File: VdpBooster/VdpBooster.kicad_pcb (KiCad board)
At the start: 2 copper layers, 36.2 x 73 mm, 30 parts, among them U1 M5M4C264L, U2 M5M4C264L, U3 M5M4C264L, U4 M5M4C264L, U5 315-5313A

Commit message: v101 changes
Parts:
- removed the C1 at (131.0, 65.5)
- removed the C2 at (137.0, 65.5)
- removed the C3 at (137.0, 53.5)
- removed the C4 at (131.0, 53.5)
- moved TP3 39.2 mm to (142.0, 13.9)
- moved TP4 35.3 mm to (145.0, 13.9)
- moved C4 32.5 mm to (138.6, 14.5), turned to 180 degrees
- moved C5 9.52 mm to (140.1, 74.5), turned to 180 degrees
- moved TP1 8.28 mm to (147.5, 87.2)
- moved TP7 8.19 mm to (133.5, 82.8)
- moved TP6 8.02 mm to (133.5, 79.8)
- moved TP5 7.98 mm to (133.5, 76.8)
- moved TP2 7.79 mm to (150.5, 87.2)
- moved R9 6.60 mm to (136.8, 83.5)
- moved C3 6.51 mm to (136.8, 82.0)
- moved R8 6.43 mm to (140.1, 83.5)
- moved R7 6.35 mm to (140.1, 82.0)
- moved R6 6.32 mm to (136.8, 80.5)
- moved C2 6.28 mm to (136.8, 79.0)
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- renumbered C6 to C1, C7 to C2, C8 to C3, C5 to C4, C9 to C5
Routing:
- net VCC: track 29.6 -> 72.8 mm, vias 0 -> 2
- net /A7: track 96.4 -> 123.9 mm, vias 2 -> 3
- net /A5: track 80.0 -> 107.1 mm, vias 1 -> 3
- net /A0: track 84.4 -> 110.9 mm
- net /A4: track 80.6 -> 106.5 mm, vias 1 -> 3
- net /A1: track 76.4 -> 102.3 mm, vias 1 -> 2
- net /A2: track 88.8 -> 111.7 mm
- net /A6: track 96.7 -> 119.3 mm, vias 1 -> 3
- net /A3: track 88.9 -> 110.5 mm
- net GND: track 36.5 -> 20.7 mm, vias 21 -> 20
- net /SC: track 78.5 -> 67.3 mm, vias 3 -> 2
- net /RD6: track 78.3 -> 69.7 mm, vias 2 -> 1
- net /RD2: track 80.0 -> 71.6 mm
- net /~{WE1}: track 56.0 -> 47.7 mm
- net /~{OE1}: track 66.8 -> 58.8 mm, vias 2 -> 1
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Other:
- board size 36.2 x 73 mm -> 34.9 x 76.4 mm
- board text added: "Analog VCC, GND⇢"
- board text added: "B"
- board text added: "G"
- board text added: "Human-made as always いつも通りAI不使用です"
- board text added: "R"
- board text added: "VDP BUDDY V1.0.1"
- board text added: "VRAM VCC, GND⇢"
- board text removed: "BLUE"
- board text removed: "GND"
- board text removed: "GNDA"
- board text removed: "GREEN"
- board text removed: "No AI/LLMs here! いつも通りAI不使用です"
- board text removed: "RED"
- board text removed: "VCC"
- board text removed: "VCCA"
- board text removed: "VDP BUDDY"
- board text removed: "←To CXA1145"

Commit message: tweaks and gerbils
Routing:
- net /SD4: track 65.2 -> 63.7 mm
- net /SD5: track 63.4 -> 62.5 mm
- net VCCA: track 30.2 -> 31.1 mm
- net /VID_B: track 8.97 -> 9.55 mm
- net /A7: track 123.9 -> 123.7 mm, vias 3 -> 2
- net GNDA: vias 16 -> 14

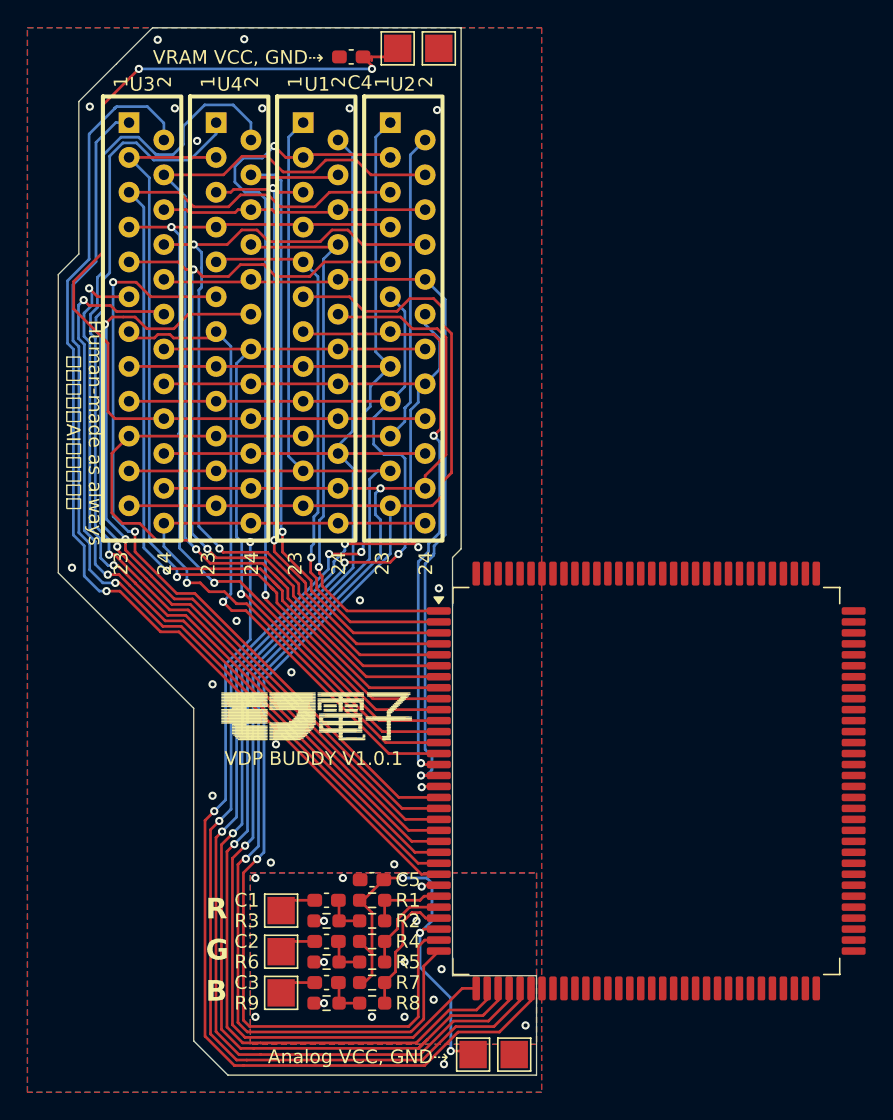
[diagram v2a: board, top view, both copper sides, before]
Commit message: Improved board layout, shrunk it and hopefully handled RGB Noise
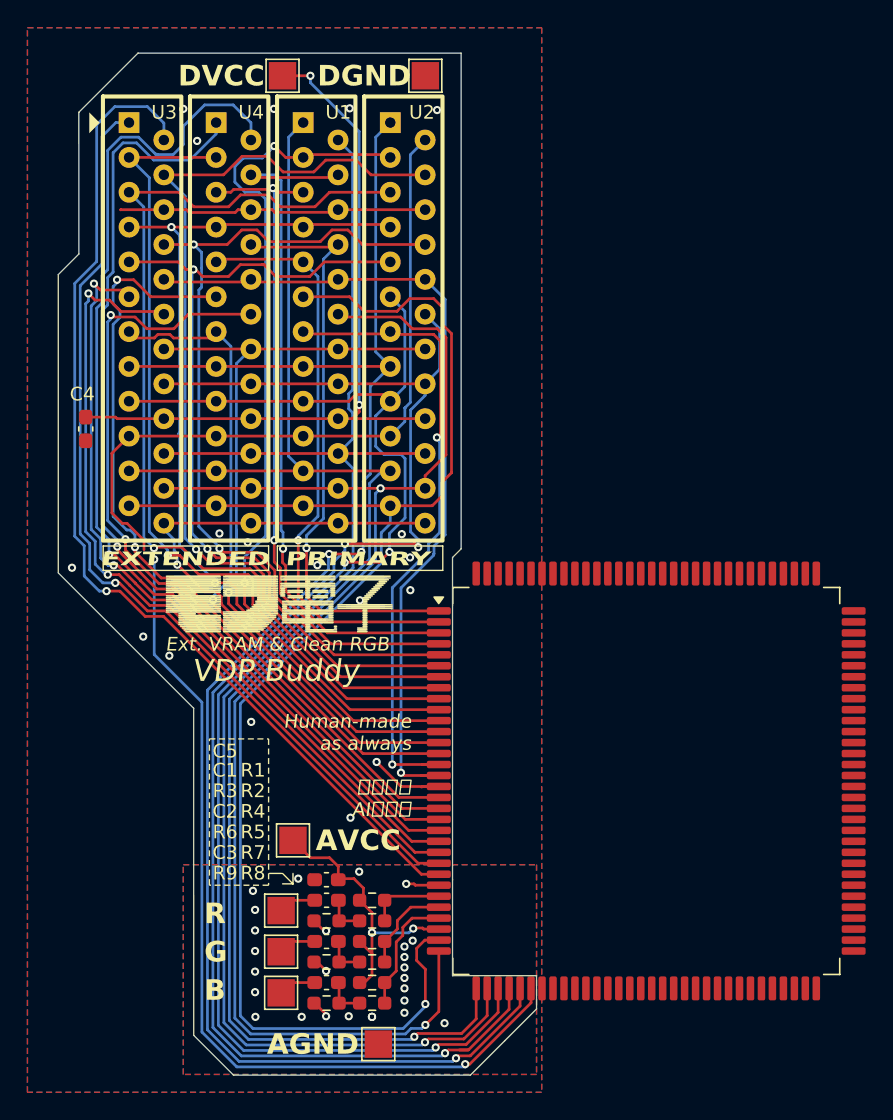
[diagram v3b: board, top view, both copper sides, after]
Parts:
- moved C4 33.3 mm to (119.3, 41.6), turned to -90 degrees
- moved TP1 20.4 mm to (134.4, 71.6)
- moved TP2 9.94 mm to (140.6, 86.5)
- moved TP3 8.63 mm to (133.6, 15.9)
- moved C5 3.32 mm to (136.8, 74.5)
- moved TP4 2.23 mm to (144.0, 15.9)
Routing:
- net VCC: track 72.8 -> 53.5 mm
- net VCCA: track 31.1 -> 21.9 mm, vias 3 -> 2
- net GND: track 20.7 -> 29.1 mm, vias 20 -> 18
- net /A7: track 123.7 -> 115.8 mm
- net GNDA: track 1.43 -> 6.69 mm, vias 14 -> 26
- net /~{WE0}: track 43.7 -> 47.5 mm
- net /~{OE1}: track 58.8 -> 61.4 mm
- net /~{SE0}: track 62.0 -> 64.3 mm
- net /SD1: track 41.1 -> 42.9 mm
- net /SD0: track 42.8 -> 44.6 mm
- net /~{RAS1}: track 56.7 -> 58.0 mm
- net /A5: track 107.1 -> 108.3 mm
- net /A3: track 110.5 -> 111.6 mm
- net /SD2: track 50.9 -> 52.0 mm
- net /~{WE1}: track 47.7 -> 48.8 mm
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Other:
- board size 34.9 x 76.4 mm -> 34.9 x 74.5 mm
- board text added: "AGND"
- board text added: "AVCC"
- board text added: "Apply insulator!"
- board text added: "Be gentle with the VDP legs!"
- board text added: "DGND"
- board text added: "DVCC"
- board text added: "EXTENDED"
- board text added: "Ext. VRAM & Clean RGB"
- board text added: "Human-made as always いつも通 AI不使用"
- board text added: "PRIMARY"
- board text added: "Raise ICs so legs are flush with bottom, not protruding. Do the first solder joint on the top side for level control."
- board text added: "VDP Buddy"
- board text removed: "Analog VCC, GND⇢"
- board text removed: "Human-made as always いつも通りAI不使用です"
- board text removed: "VDP BUDDY V1.0.1"
- board text removed: "VRAM VCC, GND⇢"
